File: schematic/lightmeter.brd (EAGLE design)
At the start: 27.9 x 52.1 mm, 80 parts, among them IC2 MCP73831/OT, J1 AVR_SPI_PRG_6NS, Q1 NCHANNELMOSFET, Q10 PCHANNELMOSFET, Q11 NCHANNELMOSFET, Q12 NCHANNELMOSFET, Q13 NCHANNELMOSFET, Q14 NCHANNELMOSFET, Q16 NCHANNELMOSFET, Q2 PCHANNELMOSFET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

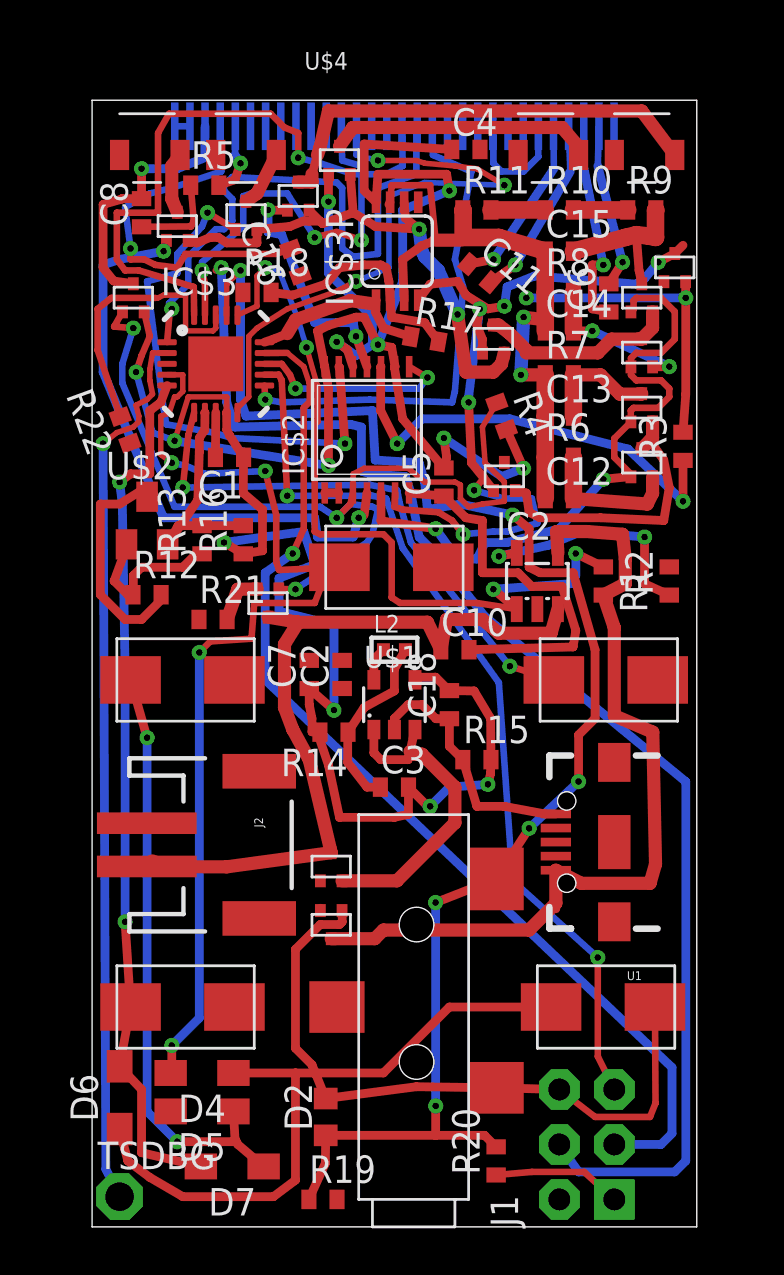
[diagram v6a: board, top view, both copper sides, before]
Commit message: More work on routing.
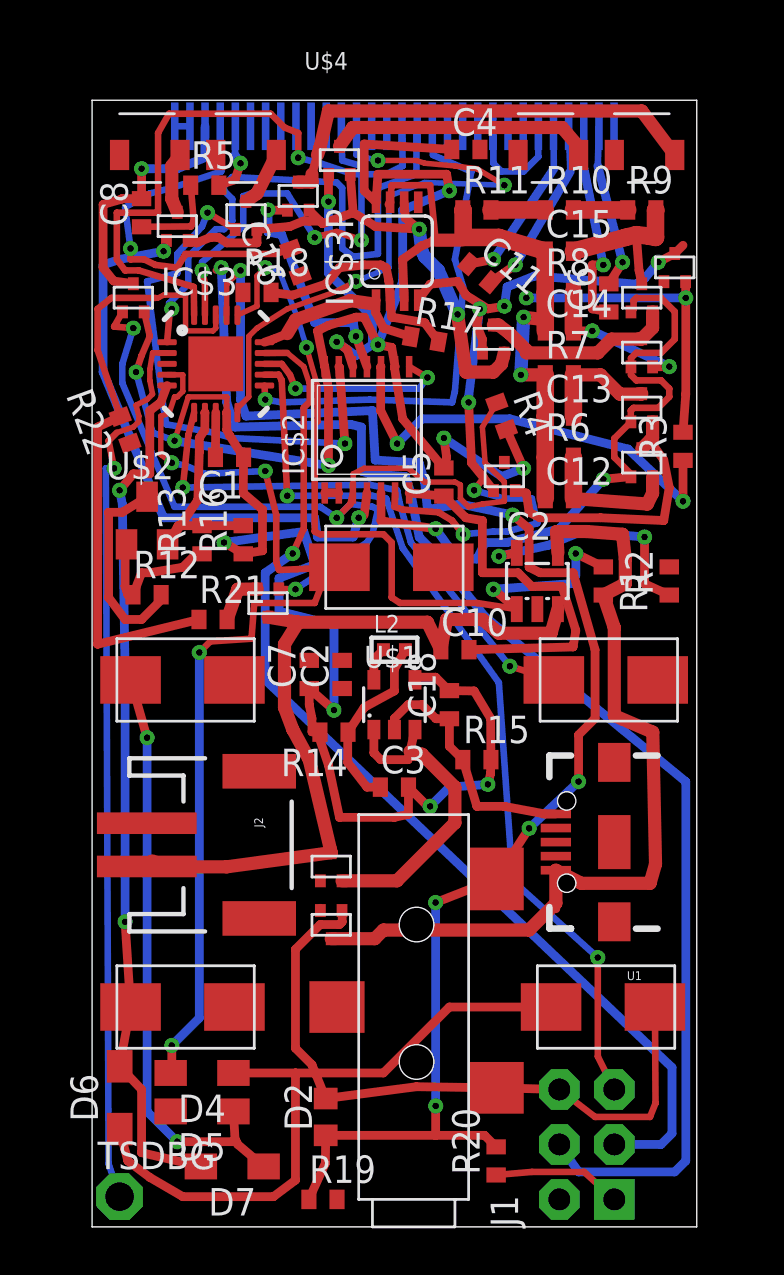
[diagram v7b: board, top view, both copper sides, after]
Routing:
- net AVRMOSI/BATVOLTAGE: track 13.1 -> 29.1 mm
- net GND: track 92.9 -> 91.7 mm
- net N$25: track 7.41 -> 6.76 mm
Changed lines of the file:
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@@
 <wire x1="1.92" y1="28.971" x2="1.016" y2="28.067" width="0.4064" layer="1"/>
 <wire x1="1.016" y1="28.067" x2="0.254" y2="28.067" width="0.4064" layer="1"/>
-<wire x1="0.254" y1="28.067" x2="-0.889" y2="29.21" width="0.4064" layer="1"/>
-<wire x1="-0.889" y1="29.21" x2="-0.889" y2="33.401" width="0.4064" layer="1"/>
-<wire x1="-0.889" y1="33.401" x2="0" y2="33.401" width="0.4064" layer="1"/>
-<wire x1="0" y1="33.401" x2="1.227" y2="34.163" width="0.4064" layer="1"/>
-<wire x1="1.227" y1="34.163" x2="1.27" y2="33.739" width="0.4064" layer="1"/>
+<wire x1="0.254" y1="28.067" x2="-0.508" y2="29.083" width="0.4064" layer="1"/>
+<wire x1="-0.508" y1="29.083" x2="-0.508" y2="33.02" width="0.4064" layer="1"/>
+<wire x1="-0.508" y1="33.02" x2="0.127" y2="33.02" width="0.4064" layer="1"/>
+<wire x1="0.127" y1="33.02" x2="1.354" y2="33.782" width="0.4064" layer="1"/>
+<wire x1="1.354" y1="33.782" x2="1.27" y2="33.739" width="0.4064" layer="1"/>
 <wire x1="14.986" y1="33.767" x2="13.38" y2="33.9122" width="0.4064" layer="1"/>
 <wire x1="26.154" y1="43.677" x2="26.162" y2="42.926" width="0.4064" layer="1"/>
@@
 <wire x1="15.85" y1="50.857" x2="16.55" y2="50.857" width="0" layer="19" extent="16-16"/>
 <wire x1="15.15" y1="50.857" x2="15.85" y2="50.857" width="0" layer="19" extent="16-16"/>
-<wire x1="16.652" y1="49.784" x2="15.85" y2="50.857" width="0" layer="19" extent="1-16"/>
-<wire x1="13.801" y1="47.347" x2="16.652" y2="49.784" width="0" layer="19" extent="1-1"/>
+<wire x1="16.652" y1="49.784" x2="16.55" y2="50.857" width="0" layer="19" extent="1-16"/>
+<wire x1="13.801" y1="47.347" x2="15.15" y2="50.857" width="0" layer="19" extent="1-16"/>
 <wire x1="8.3503125" y1="43.966196875" x2="13.801" y2="47.347" width="0" layer="19" extent="1-1"/>
 <wire x1="5.7" y1="43.18" x2="8.3503125" y2="43.966196875" width="0" layer="19" extent="1-1"/>
 <wire x1="4.445" y1="39.878" x2="5.7" y2="43.18" width="0" layer="19" extent="1-1"/>
 <wire x1="4.445" y1="37.628" x2="4.445" y2="39.878" width="0" layer="19" extent="1-1"/>
-<wire x1="1.227" y1="34.163" x2="4.43" y2="35.56" width="0" layer="19" extent="1-1"/>
-<wire x1="0.4763125" y1="36.219196875" x2="1.227" y2="34.163" width="0" layer="19" extent="1-1"/>
+<wire x1="1.354" y1="33.782" x2="4.43" y2="35.56" width="0" layer="19" extent="1-1"/>
+<wire x1="0.4763125" y1="36.219196875" x2="1.354" y2="33.782" width="0" layer="19" extent="1-1"/>
 <wire x1="3.302" y1="46.228" x2="5.7" y2="43.18" width="0" layer="19" extent="1-1"/>
 <wire x1="4.445" y1="49.53" x2="3.287" y2="48.133" width="0" layer="19" extent="1-1"/>
@@
 <wire x1="0.254" y1="14.097" x2="0.254" y2="25.781" width="0.4064" layer="16"/>
 <wire x1="0.254" y1="25.781" x2="0.127" y2="33.401" width="0.4064" layer="16"/>
-<wire x1="0.127" y1="33.401" x2="0" y2="34.417" width="0.4064" layer="16"/>
-<via x="0" y="34.417" extent="1-16" drill="0.3" shape="square"/>
-<wire x1="0" y1="34.417" x2="0.508" y2="34.798" width="0.4064" layer="1"/>
-<wire x1="0.508" y1="34.798" x2="1.397" y2="34.798" width="0.4064" layer="1"/>
+<wire x1="0.127" y1="33.401" x2="0" y2="34.036" width="0.4064" layer="16"/>
+<via x="0" y="34.036" extent="1-16" drill="0.3" shape="square"/>
+<wire x1="0" y1="34.036" x2="0.635" y2="34.798" width="0.4064" layer="1"/>
+<wire x1="0.635" y1="34.798" x2="1.397" y2="34.798" width="0.4064" layer="1"/>
 <wire x1="1.397" y1="34.798" x2="1.397" y2="37.719" width="0.4064" layer="1"/>
 <wire x1="2.195" y1="38.877240625" x2="1.905" y2="38.1" width="0.4064" layer="1"/>
@@
 <wire x1="1.397" y1="39.624" x2="1.397" y2="39.116" width="0.254" layer="1"/>
 <wire x1="1.397" y1="39.116" x2="1.524" y2="38.481" width="0.254" layer="1"/>
-<via x="-0.762" y="36.195" extent="1-16" drill="0.3" shape="square"/>
-<wire x1="-0.762" y1="36.195" x2="-0.635" y2="2.667" width="0.4064" layer="16"/>
-<wire x1="-0.635" y1="2.667" x2="0" y2="1.397" width="0.4064" layer="16"/>
 <wire x1="0.635" y1="36.957" x2="-0.127" y2="36.703" width="0.254" layer="1"/>
-<wire x1="-0.127" y1="36.703" x2="-0.762" y2="36.195" width="0.254" layer="1"/>
 <wire x1="1.524" y1="38.481" x2="1.27" y2="38.227" width="0.254" layer="1"/>
 <wire x1="1.27" y1="38.227" x2="0.762" y2="37.973" width="0.254" layer="1"/>
@@
 <wire x1="0.889" y1="37.465" x2="0.889" y2="37.211" width="0.254" layer="1"/>
 <wire x1="0.889" y1="37.211" x2="0.635" y2="36.957" width="0.254" layer="1"/>
+<wire x1="-0.127" y1="36.703" x2="-0.508" y2="36.322" width="0.3048" layer="1"/>
+<wire x1="-0.508" y1="36.322" x2="-0.254" y2="35.052" width="0.3048" layer="1"/>
+<via x="-0.254" y="35.052" extent="1-16" drill="0.3" shape="square"/>
+<wire x1="-0.254" y1="35.052" x2="-0.635" y2="35.052" width="0.3048" layer="16"/>
+<wire x1="-0.635" y1="35.052" x2="-0.508" y2="2.921" width="0.3048" layer="16"/>
+<wire x1="-0.508" y1="2.921" x2="0" y2="1.397" width="0.3048" layer="16"/>
 </signal>
 <signal name="SCRVREG">
@@
 <wire x1="3.81" y1="31.1" x2="3.541" y2="31.1" width="0.4064" layer="1"/>
 <wire x1="3.541" y1="31.1" x2="2.921" y2="30.48" width="0.4064" layer="1"/>
-<wire x1="2.921" y1="30.48" x2="1.016" y2="30.48" width="0.4064" layer="1"/>
-<wire x1="1.016" y1="30.48" x2="0.635" y2="30.099" width="0.4064" layer="1"/>
-<wire x1="0.635" y1="30.099" x2="0.635" y2="29.225" width="0.4064" layer="1"/>
+<wire x1="2.921" y1="30.48" x2="1.397" y2="30.226" width="0.4064" layer="1"/>
+<wire x1="1.397" y1="30.226" x2="1.016" y2="30.226" width="0.4064" layer="1"/>
+<wire x1="1.016" y1="30.226" x2="0.635" y2="29.225" width="0.4064" layer="1"/>
 <wire x1="0.635" y1="29.225" x2="0.62" y2="29.21" width="0.4064" layer="1"/>
 <wire x1="0.62" y1="29.21" x2="0.381" y2="29.21" width="0.4064" layer="1"/>
-<wire x1="0.381" y1="29.21" x2="-0.254" y2="29.845" width="0.4064" layer="1"/>
-<wire x1="-0.254" y1="29.845" x2="0.254" y2="31.219" width="0.4064" layer="1"/>
+<wire x1="0.381" y1="29.21" x2="0.254" y2="29.591" width="0.4064" layer="1"/>
+<wire x1="0.254" y1="29.591" x2="0.254" y2="31.219" width="0.4064" layer="1"/>
 <wire x1="0.254" y1="31.219" x2="0.32" y2="31.539" width="0.4064" layer="1"/>
 </signal>
@@
 <wire x1="4.318" y1="41.402" x2="4.445" y2="41.529" width="0.254" layer="1"/>
 <wire x1="4.445" y1="41.529" x2="4.445" y2="42.128" width="0.254" layer="1"/>
-<wire x1="3.668" y1="28.067" x2="0.031684375" y2="37.4408" width="0" layer="19" extent="1-1"/>
+<wire x1="3.668" y1="28.067" x2="-1.016" y2="26.924" width="0.4064" layer="1"/>
+<wire x1="-1.016" y1="26.924" x2="-1.016" y2="36.957" width="0.4064" layer="1"/>
+<wire x1="-1.016" y1="36.957" x2="0.031684375" y2="37.4408" width="0.4064" layer="1"/>
 </signal>
 <signal name="N$30">

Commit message: Routing -ground almost all done.
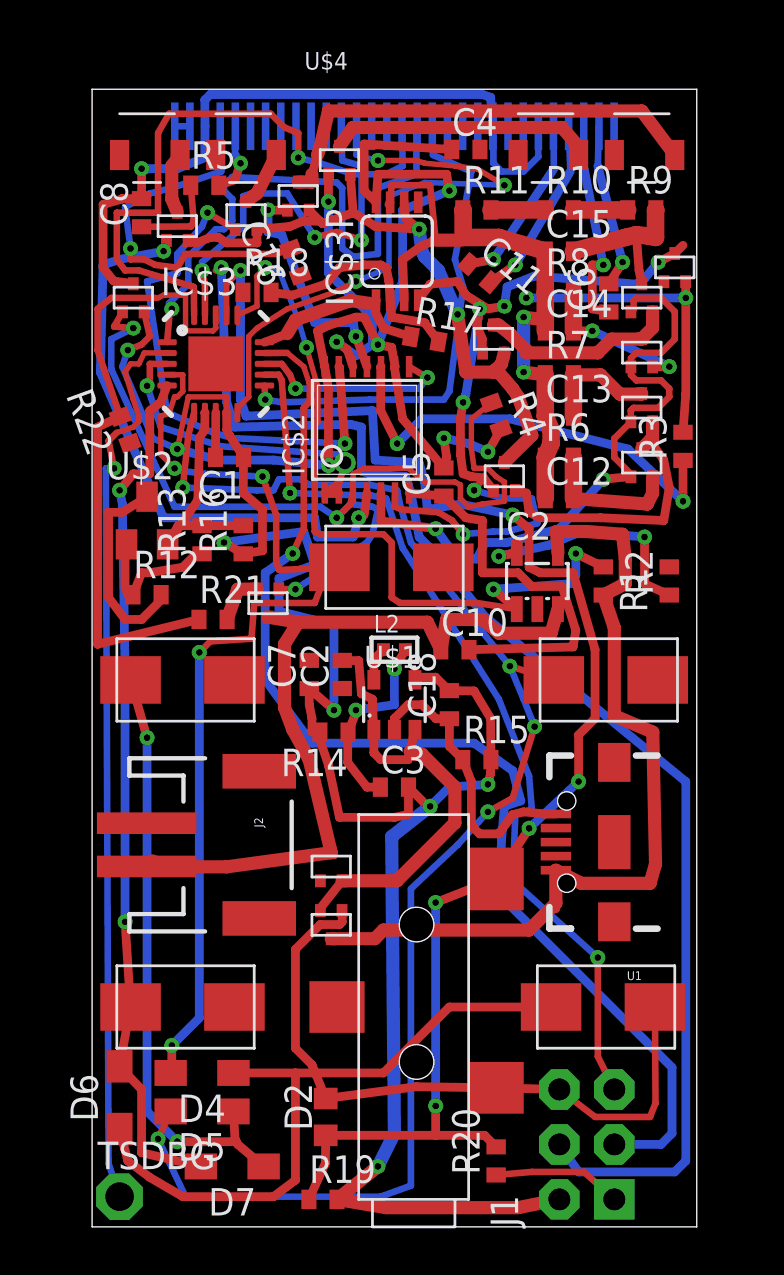
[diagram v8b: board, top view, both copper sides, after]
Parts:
- moved R4 0.25 mm to (17.4, 37.5)
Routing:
- net PBI$3: track 25.4 -> 67.2 mm, vias 2 -> 5
- net VREG: track 113.0 -> 141.9 mm, vias 11 -> 12
- net SCRVREG: track 18.0 -> 33.9 mm
- net SRA: track 0.65 -> 15.1 mm, vias 0 -> 2
- net VCC: track 15.1 -> 20.9 mm
- net N$26: track 25.3 -> 30.6 mm
- net AVRSCK: track 49.3 -> 54.3 mm
- net GND: track 91.7 -> 93.4 mm
- net SCRPWR: track 42.2 -> 43.8 mm
- net STG$2: track 23.2 -> 23.9 mm
- net N$17: track 8.46 -> 9.03 mm, vias 0 -> 2
- net N$23: track 41.4 -> 42.0 mm
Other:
- board size 27.9 x 52.1 mm -> 27.9 x 52.6 mm
